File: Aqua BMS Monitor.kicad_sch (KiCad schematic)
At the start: 162 parts, among them J4 Conn_01x04, J5 Conn_01x04, Q1 NMOS, Q10 NMOS, Q11 NMOS, Q13 NMOS, Q14 NMOS, Q2 PMOS, Q3 PMOS, Q4 NMOS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

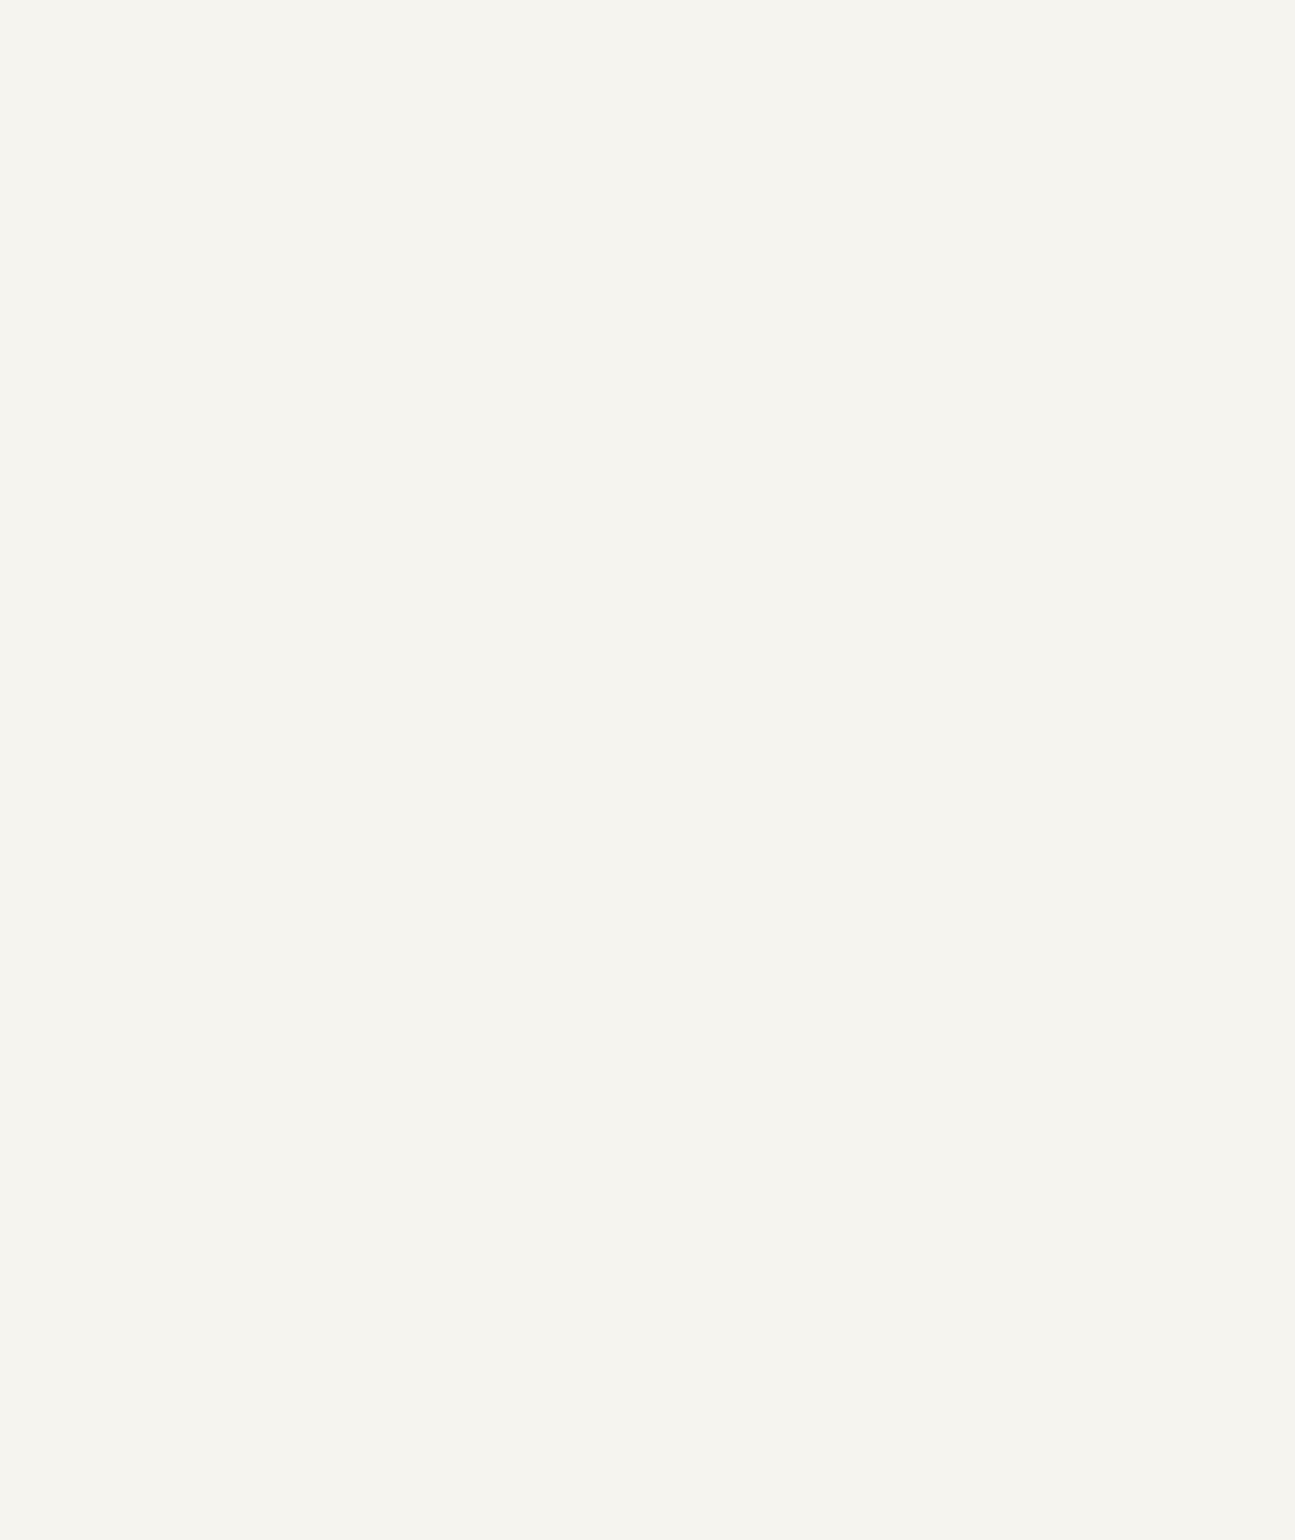
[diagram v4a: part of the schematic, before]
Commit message: Update Aqua BMS Monitor.kicad_sch
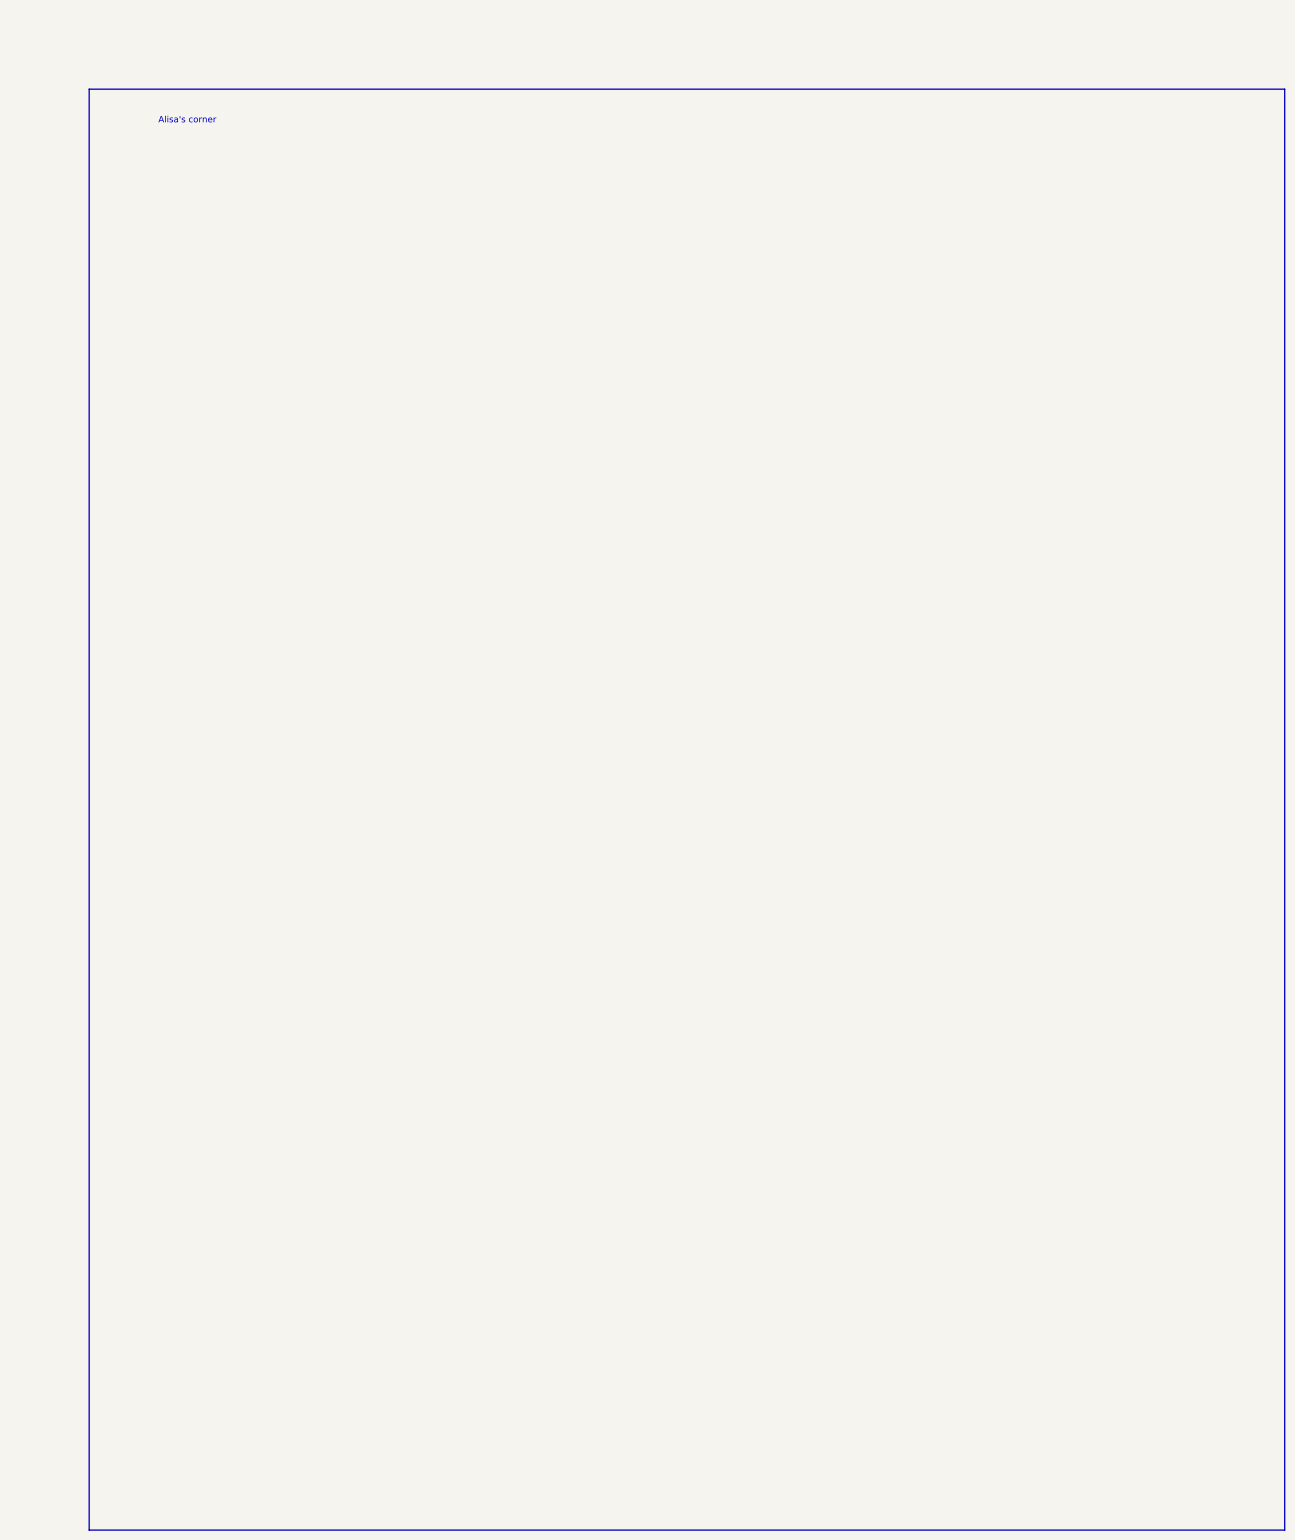
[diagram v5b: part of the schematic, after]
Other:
- note added: "Alisa's corner"
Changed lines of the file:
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@@
+	)
+	(rectangle
+		(start 558.8 255.27)
+		(end 800.1 546.1)
+		(stroke
+			(width 0)
+			(type default)
+		)
+		(fill
+			(type none)
+		)
 	)
 	(rectangle
@@
 		(effects
 			(font
+				(size 1.27 1.27)
+			)
+		)
+	)
+	(text "Alisa's corner"
+		(exclude_from_sim no)
+		(at 578.612 261.62 0)
+		(effects
+			(font
